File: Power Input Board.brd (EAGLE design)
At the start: 136.7 x 125.3 mm, 19 parts, among them Q1 SPB80P06P

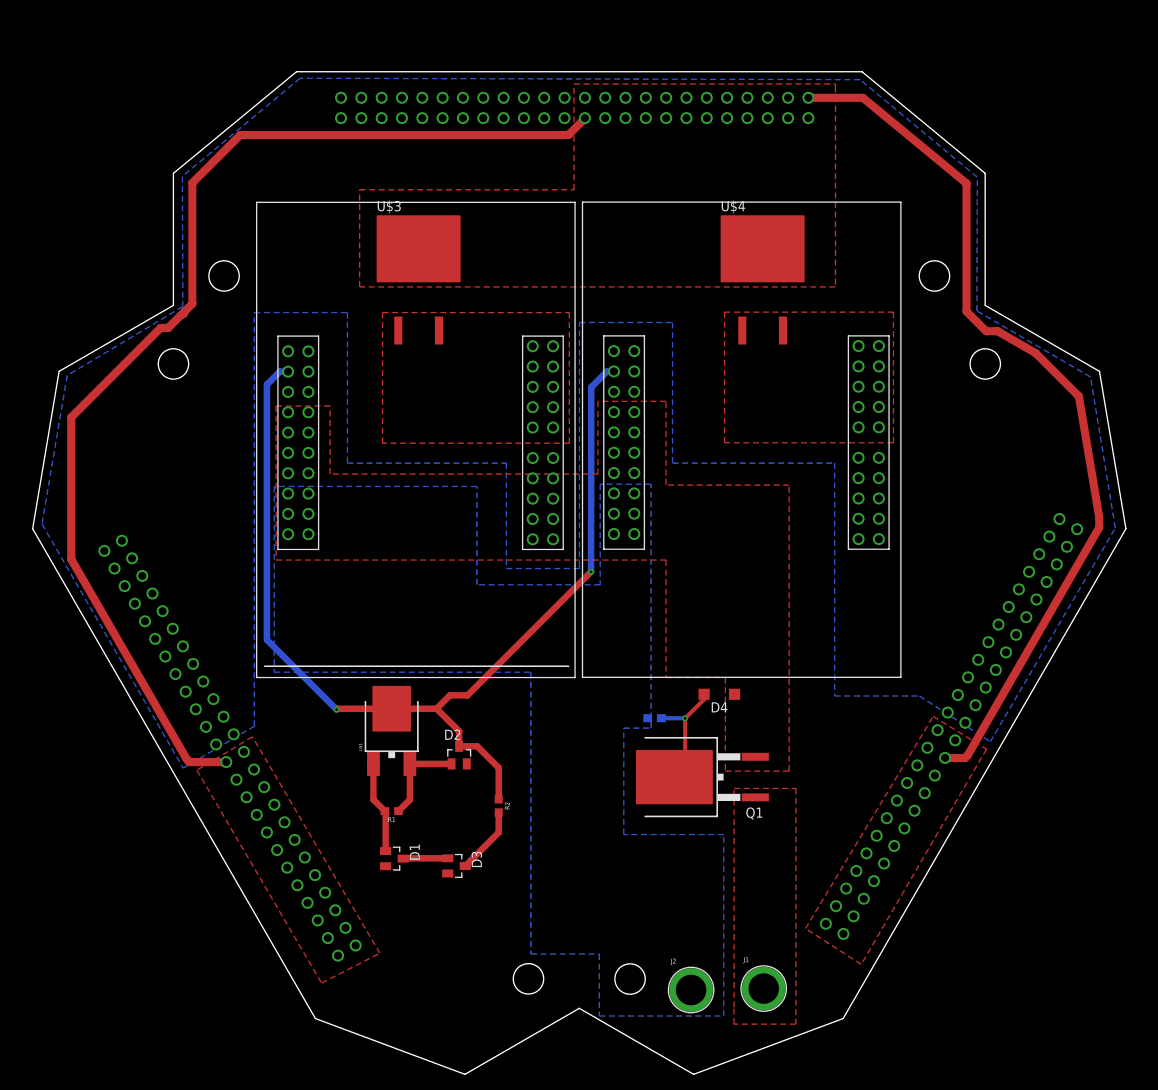
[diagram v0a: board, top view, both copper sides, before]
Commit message: took off the dumb lines
took off the routed lines that wouldve popped off the board
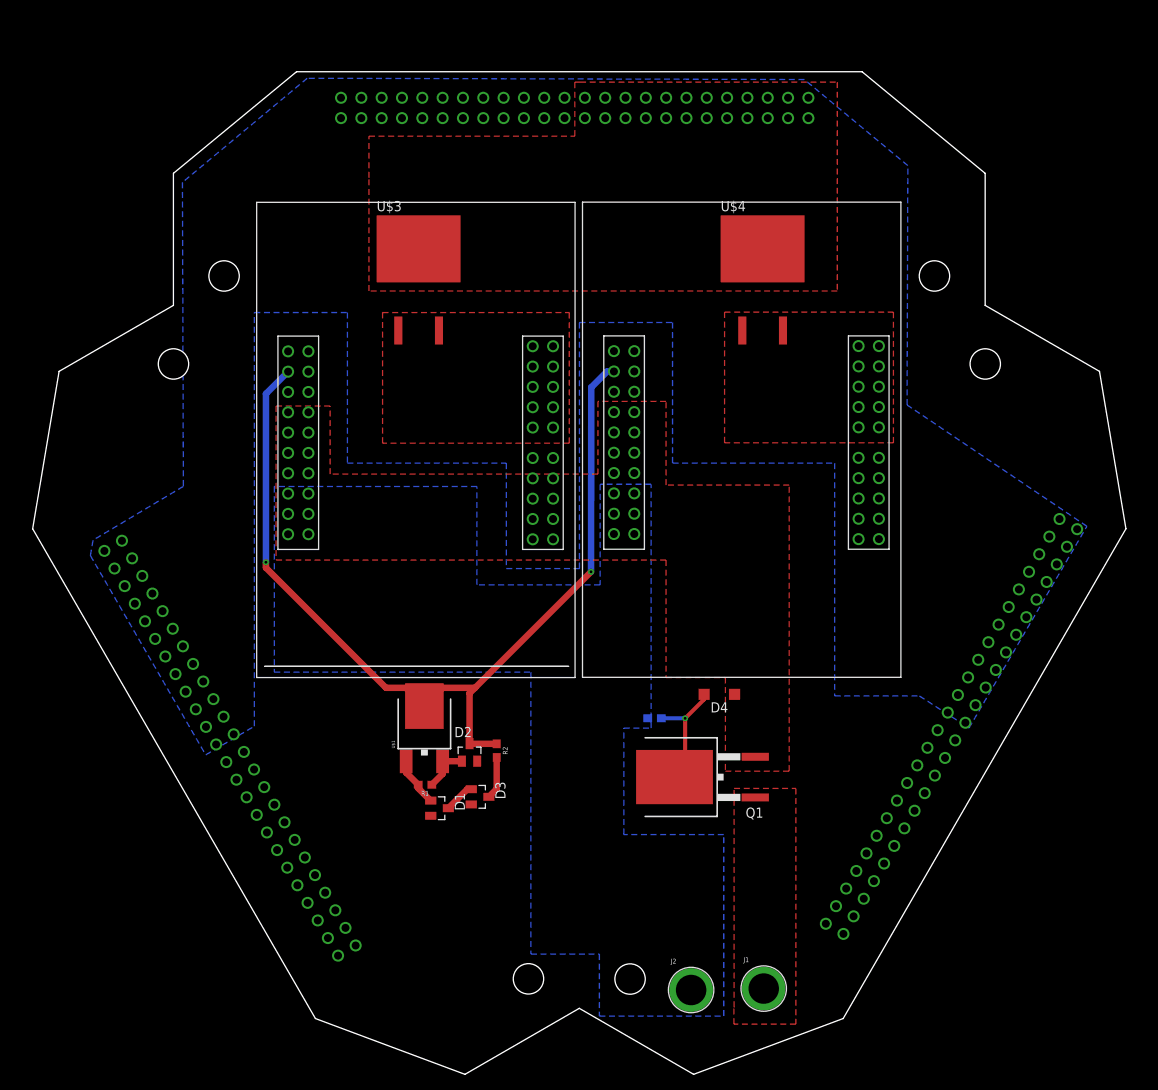
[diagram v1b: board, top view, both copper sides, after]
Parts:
- moved D3 9.12 mm to (55.9, 34.7)
- moved D1 8.45 mm to (50.9, 33.3)
- moved R2 6.91 mm to (58.0, 40.5)
- moved R1 5.32 mm to (49.0, 36.2)
- moved U$1 4.10 mm to (49.0, 44.4)
- moved D2 1.34 mm to (54.6, 40.2)
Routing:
- net +12V: track 250.4 -> 0.00 mm
- net ON/OFF: track 129.0 -> 117.9 mm
- net 3.3V: track 11.7 -> 5.91 mm
- net N$2: track 11.5 -> 6.19 mm
- net N$5: track 8.38 -> 5.33 mm
- net N$1: track 5.58 -> 3.85 mm

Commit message: fixed some stuff
moved things around
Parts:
- moved J2 30.2 mm to (52.2, 11.3)
- moved D2 13.5 mm to (54.3, 53.7)
- moved D3 13.5 mm to (55.6, 48.1)
- moved R2 13.5 mm to (57.7, 53.9)
- moved U$1 13.5 mm to (48.6, 57.9)
- moved D1 13.5 mm to (50.5, 46.7)
- moved R1 13.5 mm to (48.7, 49.7)
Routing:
- net ON/OFF: track 117.9 -> 99.6 mm
- net N$5: track 5.33 -> 0.00 mm
- net N$1: track 3.85 -> 0.00 mm

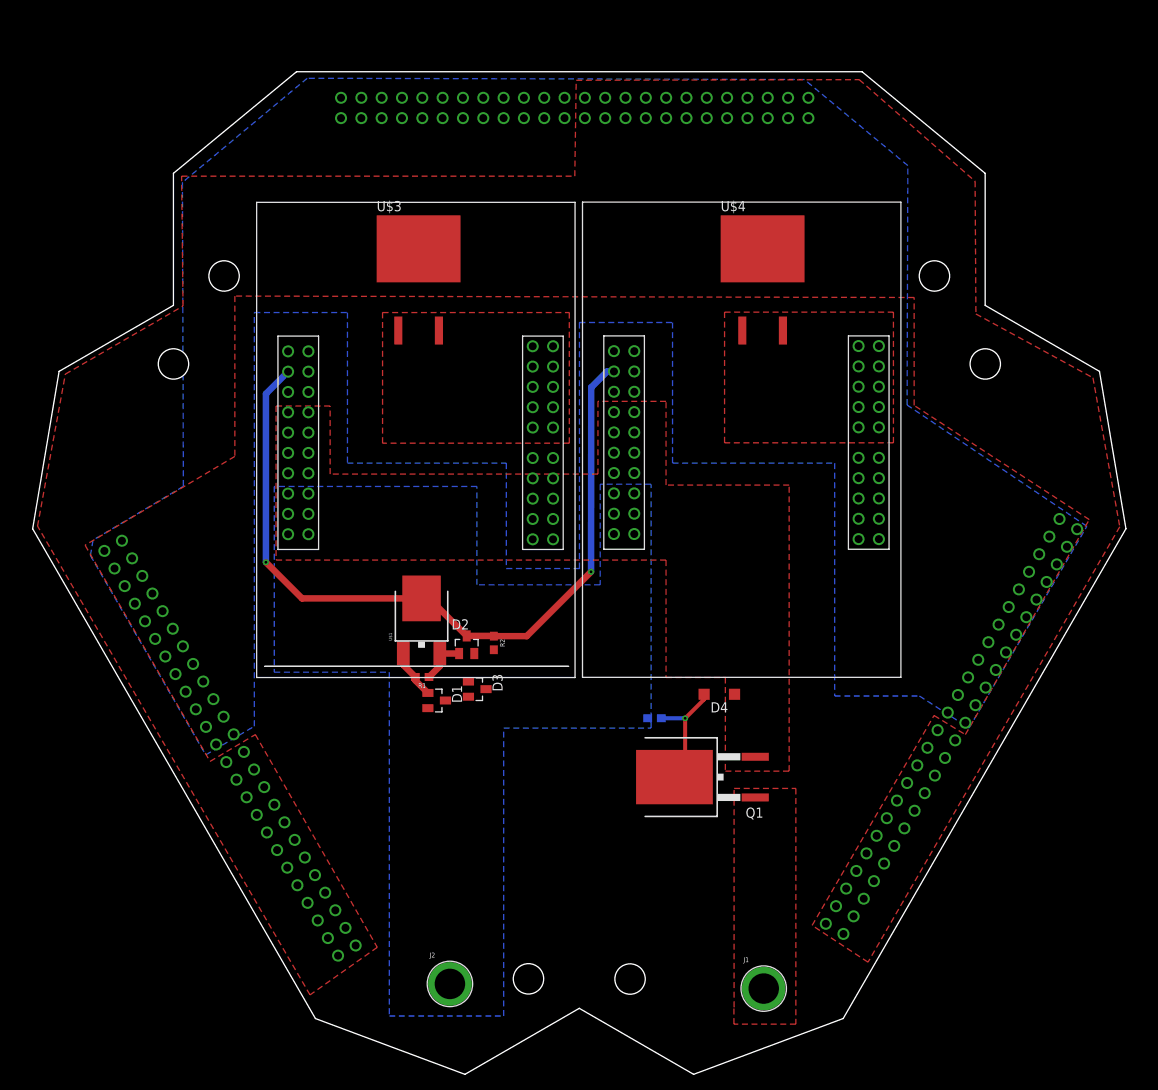
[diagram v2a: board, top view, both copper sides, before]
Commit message: rerouted
repositioned the polygons and rerouted the components
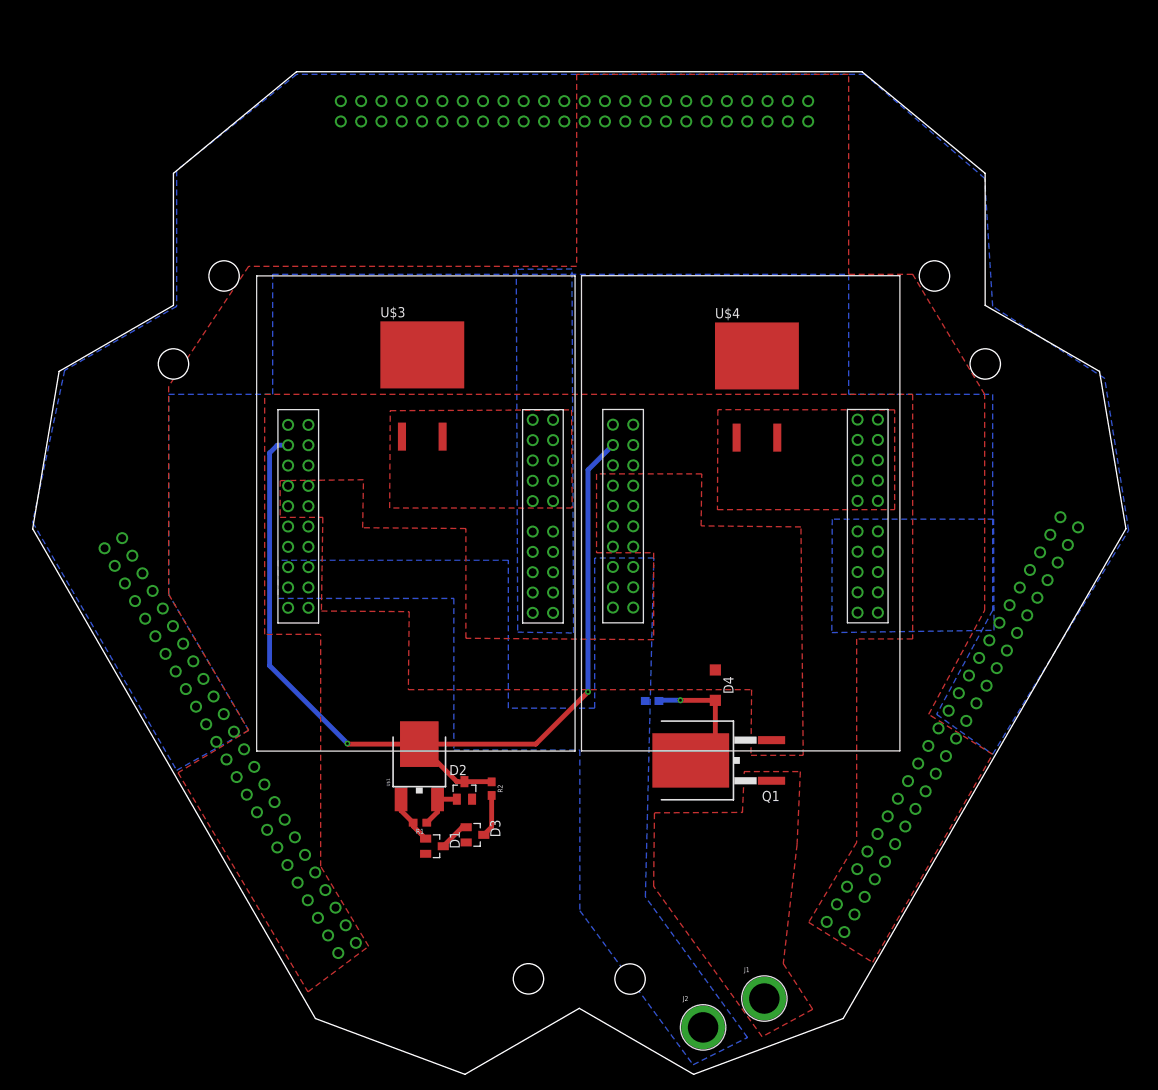
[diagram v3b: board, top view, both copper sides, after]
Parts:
- moved J2 32.1 mm to (83.8, 5.87)
- moved R2 18.2 mm to (57.4, 35.7)
- moved U$1 18.2 mm to (48.3, 39.7)
- moved D1 18.2 mm to (50.2, 28.5)
- moved D3 18.2 mm to (55.3, 29.9)
- moved D2 18.2 mm to (54.0, 35.5)
- moved R1 18.2 mm to (48.4, 31.5)
- moved U$4 13.4 mm to (85.3, 85.6)
- moved U$3 13.3 mm to (43.5, 85.7)
- moved U$6 9.20 mm to (68.6, 99.8)
- moved U$5 9.19 mm to (28.0, 99.8)
- moved Q1 2.91 mm to (85.8, 39.2)
- moved R3 2.18 mm to (77.4, 46.7)
- moved J1 1.25 mm to (91.5, 9.48)
- moved D4 1.25 mm to (85.3, 48.6), turned to 270 degrees
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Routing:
- net ON/OFF: track 99.6 -> 119.0 mm
- net N$5: track 0.00 -> 5.33 mm
- net N$1: track 0.00 -> 3.85 mm
- net N$3: track 14.9 -> 15.9 mm

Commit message: rerouted
rerouted the whole board
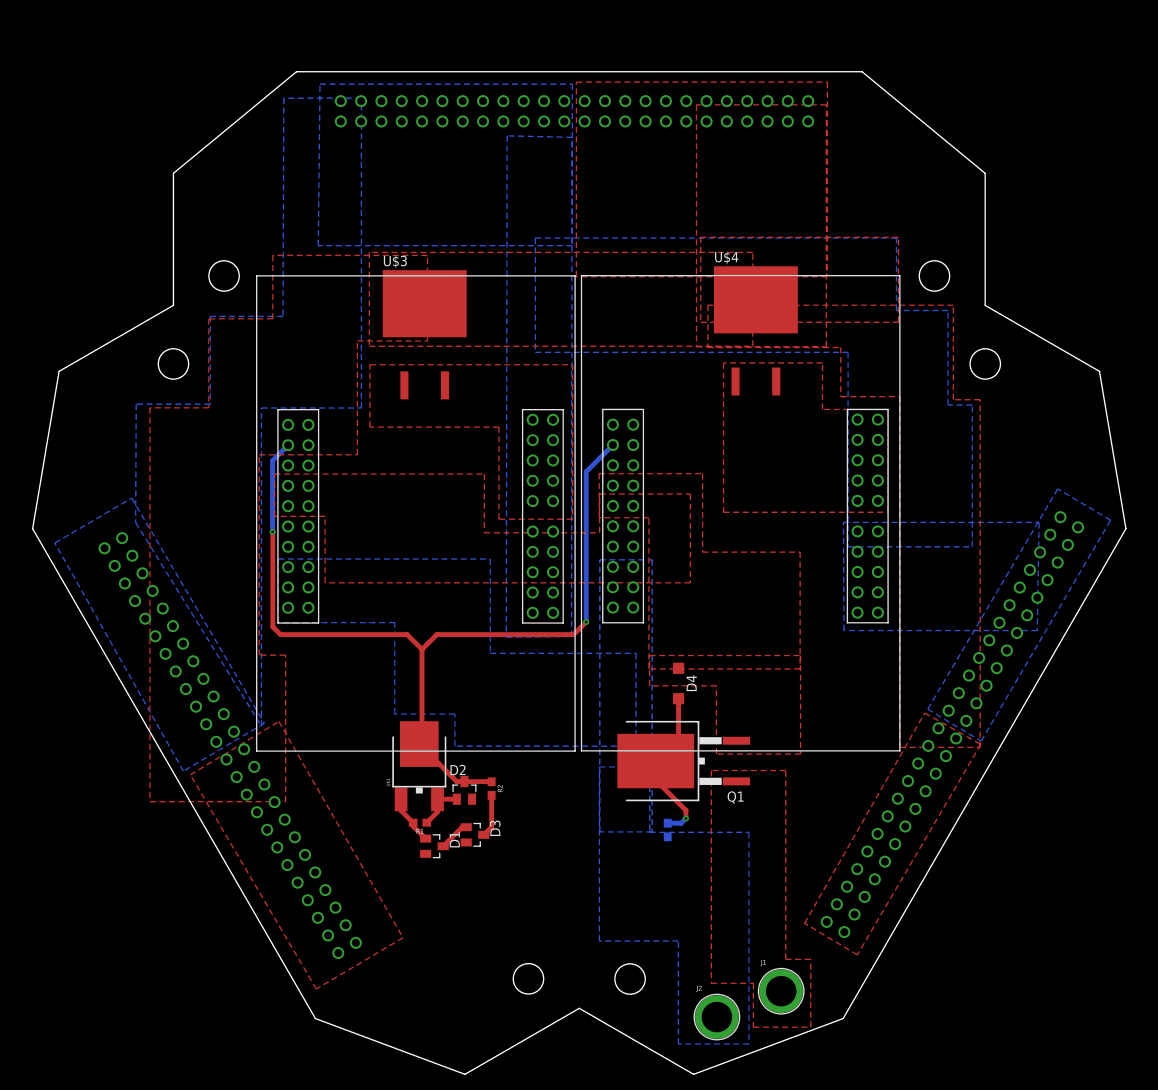
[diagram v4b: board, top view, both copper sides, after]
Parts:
- moved R3 16.3 mm to (79.4, 30.5), turned to 90 degrees
- moved U$4 7.01 mm to (85.2, 92.6)
- moved U$3 6.41 mm to (43.8, 92.1)
- moved D4 4.60 mm to (80.7, 48.9)
- moved Q1 4.37 mm to (81.4, 39.2)
- moved J1 2.30 mm to (93.6, 10.4)
- moved J2 2.16 mm to (85.5, 7.16)
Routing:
- net ON/OFF: track 119.0 -> 111.9 mm
- net N$3: track 15.9 -> 20.2 mm

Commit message: rerouted
rerouted everything
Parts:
- removed U$8, U$9: PDB_PCB_CONNEC, PDB_PCB_connectors:PDB_PCB
- U$7: device PDB_PCB_connectors:PDB_PCB -> PDB_PCB_connectors:PDB_PCB_2
- moved U$7 50.1 mm to (0.00, 0.00), turned to 0 degrees
- moved D3 11.2 mm to (59.7, 19.7)
- moved D2 11.0 mm to (57.6, 25.1)
- moved U$4 10.9 mm to (93.1, 85.1)
- moved R2 10.9 mm to (60.8, 25.4)
- moved U$3 10.1 mm to (51.0, 85.1)
- moved R3 8.32 mm to (71.4, 28.4), turned to 180 degrees
- moved R1 8.32 mm to (52.2, 24.1)
- moved U$1 8.32 mm to (52.1, 32.3)
- moved D1 8.23 mm to (52.5, 20.6)
- moved D4 7.11 mm to (82.7, 42.0), turned to 180 degrees
- moved J2 3.99 mm to (81.6, 6.70)
- moved J1 3.79 mm to (90.4, 8.28)
- moved Q1 3.22 mm to (80.7, 36.0)
- moved U$6 1.81 mm to (69.3, 98.2)
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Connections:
- net +12V: now also U$7.+12V25, U$7.+12V26, U$7.+12V27, U$7.+12V28, U$7.+12V29, U$7.+12V30, U$7.+12V31, U$7.+12V32, U$7.+12V33, U$7.+12V34, U$7.+12V35, U$7.+12V36, U$7.+12V37, U$7.+12V38, U$7.+12V39, U$7.+12V40, U$7.+12V41, U$7.+12V42, U$7.+12V43, U$7.+12V44, U$7.+12V45, U$7.+12V46, U$7.+12V47, U$7.+12V48, U$7.+12V49, U$7.+12V50, U$7.+12V51, U$7.+12V52, U$7.+12V53, U$7.+12V54, U$7.+12V55, U$7.+12V56, U$7.+12V57, U$7.+12V58, U$7.+12V59, U$7.+12V60, U$7.+12V61, U$7.+12V62, U$7.+12V63, U$7.+12V64, U$7.+12V65, U$7.+12V66, U$7.+12V67, U$7.+12V68, U$7.+12V69, U$7.+12V70, U$7.+12V71, U$7.+12V72; no longer U$8.+12V1, U$8.+12V10, U$8.+12V11, U$8.+12V12, U$8.+12V13, U$8.+12V14, U$8.+12V15, U$8.+12V16, U$8.+12V17, U$8.+12V18, U$8.+12V19, U$8.+12V2, U$8.+12V20, U$8.+12V21, U$8.+12V22, U$8.+12V23, U$8.+12V24, U$8.+12V3, U$8.+12V4, U$8.+12V5, U$8.+12V6, U$8.+12V7, U$8.+12V8, U$8.+12V9, U$9.+12V1, U$9.+12V10, U$9.+12V11, U$9.+12V12, U$9.+12V13, U$9.+12V14, U$9.+12V15, U$9.+12V16, U$9.+12V17, U$9.+12V18, U$9.+12V19, U$9.+12V2, U$9.+12V20, U$9.+12V21, U$9.+12V22, U$9.+12V23, U$9.+12V24, U$9.+12V3, U$9.+12V4, U$9.+12V5, U$9.+12V6, U$9.+12V7, U$9.+12V8, U$9.+12V9
- net GND: now also U$7.GND1, U$7.GND25, U$7.GND26, U$7.GND27, U$7.GND28, U$7.GND29, U$7.GND30, U$7.GND31, U$7.GND32, U$7.GND33, U$7.GND34, U$7.GND35, U$7.GND36, U$7.GND37, U$7.GND38, U$7.GND39, U$7.GND40, U$7.GND41, U$7.GND42, U$7.GND43, U$7.GND44, U$7.GND45, U$7.GND46, U$7.GND47, U$7.GND48, U$7.GND49, U$7.GND50, U$7.GND51, U$7.GND52, U$7.GND53, U$7.GND54, U$7.GND55, U$7.GND56, U$7.GND57, U$7.GND58, U$7.GND59, U$7.GND60, U$7.GND61, U$7.GND62, U$7.GND63, U$7.GND64, U$7.GND65, U$7.GND66, U$7.GND67, U$7.GND68, U$7.GND69, U$7.GND70, U$7.GND71, U$7.GND72; no longer U$8.GND10, U$8.GND11, U$8.GND12, U$8.GND13, U$8.GND14, U$8.GND15, U$8.GND16, U$8.GND17, U$8.GND18, U$8.GND19, U$8.GND2, U$8.GND20, U$8.GND21, U$8.GND22, U$8.GND23, U$8.GND24, U$8.GND3, U$8.GND4, U$8.GND5, U$8.GND6, U$8.GND7, U$8.GND8, U$8.GND9, U$9.GND10, U$9.GND11, U$9.GND12, U$9.GND13, U$9.GND14, U$9.GND15, U$9.GND16, U$9.GND17, U$9.GND18, U$9.GND19, U$9.GND2, U$9.GND20, U$9.GND21, U$9.GND22, U$9.GND23, U$9.GND24, U$9.GND3, U$9.GND4, U$9.GND5, U$9.GND6, U$9.GND7, U$9.GND8, U$9.GND9
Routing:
- net ON/OFF: track 111.9 -> 127.8 mm
- net N$3: track 20.2 -> 18.4 mm
- net N$1: track 3.85 -> 5.08 mm
- net 3.3V: track 5.90 -> 7.08 mm

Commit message: Added some silkscreen
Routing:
- net ON/OFF: track 127.8 -> 124.7 mm
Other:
- board text added: "+48V"
- board text added: "48V_GND"
- board text added: "Power Distribution Board v1.0 Jan 2019 Cynthia Zatlokowicz Jason King"
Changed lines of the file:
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@@
 <?xml version="1.0" encoding="utf-8"?>
 <!DOCTYPE eagle SYSTEM "eagle.dtd">
-<eagle version="9.2.0">
+<eagle version="9.1.3">
 <drawing>
 <settings>
@@
 <board>
 <plain>
+<text x="87.5284" y="12.6238" size="1.778" layer="21">+48V</text>
+<text x="82.0166" y="11.2014" size="1.778" layer="21" rot="R90">48V_GND</text>
+<text x="73.4314" y="101.981" size="1.778" layer="21">Power Distribution Board v1.0
+Jan 2019
+Cynthia Zatlokowicz
+Jason King</text>
 </plain>
 <attributes>
@@
 <wire x1="57.5818" y1="26.2262" x2="57.5818" y2="28.449" width="0.8128" layer="1"/>
 <wire x1="57.5818" y1="28.449" x2="52.1416" y2="33.8892" width="0.8128" layer="1"/>
-<wire x1="52.1416" y1="33.8892" x2="49.149" y2="36.8818" width="0.8128" layer="1"/>
 <via x="30.2514" y="54.0512" extent="1-16" drill="0.35"/>
-<wire x1="49.149" y1="36.8818" x2="31.9796" y2="54.0512" width="0.8128" layer="1"/>
-<wire x1="31.9796" y1="54.0512" x2="30.2514" y2="54.0512" width="0.8128" layer="1"/>
 <wire x1="30.2514" y1="54.0512" x2="30.2514" y2="75.1836" width="0.8128" layer="16"/>
 <wire x1="30.2514" y1="75.1836" x2="32.1586" y2="77.0908" width="0.8128" layer="16"/>
-<via x="49.1744" y="52.5272" extent="1-16" drill="0.35"/>
 <wire x1="67.0306" y1="52.5272" x2="49.1744" y2="52.5272" width="0.8128" layer="16"/>
 <wire x1="67.0306" y1="52.5272" x2="68.6054" y2="54.102" width="0.8128" layer="16"/>
 <wire x1="68.6054" y1="54.102" x2="68.6054" y2="72.3504" width="0.8128" layer="16"/>
 <wire x1="68.6054" y1="72.3504" x2="73.2696" y2="77.0146" width="0.8128" layer="16"/>
-<wire x1="49.1744" y1="52.5272" x2="49.149" y2="52.5018" width="0.8128" layer="1"/>
-<wire x1="49.149" y1="52.5018" x2="49.149" y2="36.8818" width="0.8128" layer="1"/>
 <wire x1="57.5818" y1="26.2262" x2="57.584" y2="26.224" width="0.8128" layer="1"/>
 <wire x1="57.584" y1="26.224" x2="60.8252" y2="26.224" width="0.8128" layer="1"/>
+<wire x1="52.1416" y1="33.8892" x2="41.0972" y2="44.9336" width="0.8128" layer="1"/>
+<wire x1="41.0972" y1="44.9336" x2="41.0972" y2="52.5526" width="0.8128" layer="1"/>
+<wire x1="41.0972" y1="52.5526" x2="31.75" y2="52.5526" width="0.8128" layer="1"/>
+<wire x1="31.75" y1="52.5526" x2="30.2514" y2="54.0512" width="0.8128" layer="1"/>
+<wire x1="41.0972" y1="52.5526" x2="49.149" y2="52.5526" width="0.8128" layer="1"/>
+<wire x1="49.149" y1="52.5526" x2="49.1744" y2="52.5272" width="0.8128" layer="1"/>
+<via x="49.1744" y="52.5272" extent="1-16" drill="0.45"/>
 </signal>
 <signal name="N$5">
@@
 </drawing>
 <compatibility>
+<note version="6.3" minversion="6.2.2" severity="warning">
+Since Version 6.2.2 text objects can contain more than one line,
+which will not be processed correctly with this version.
+</note>
 <note version="8.2" severity="warning">
 Since Version 8.2, EAGLE supports online libraries. The ids
